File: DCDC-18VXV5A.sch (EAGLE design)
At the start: 36 parts, among them Q10 NMOSFET, Q9 NMOSFET, U1 LM3150MHX/NOPB

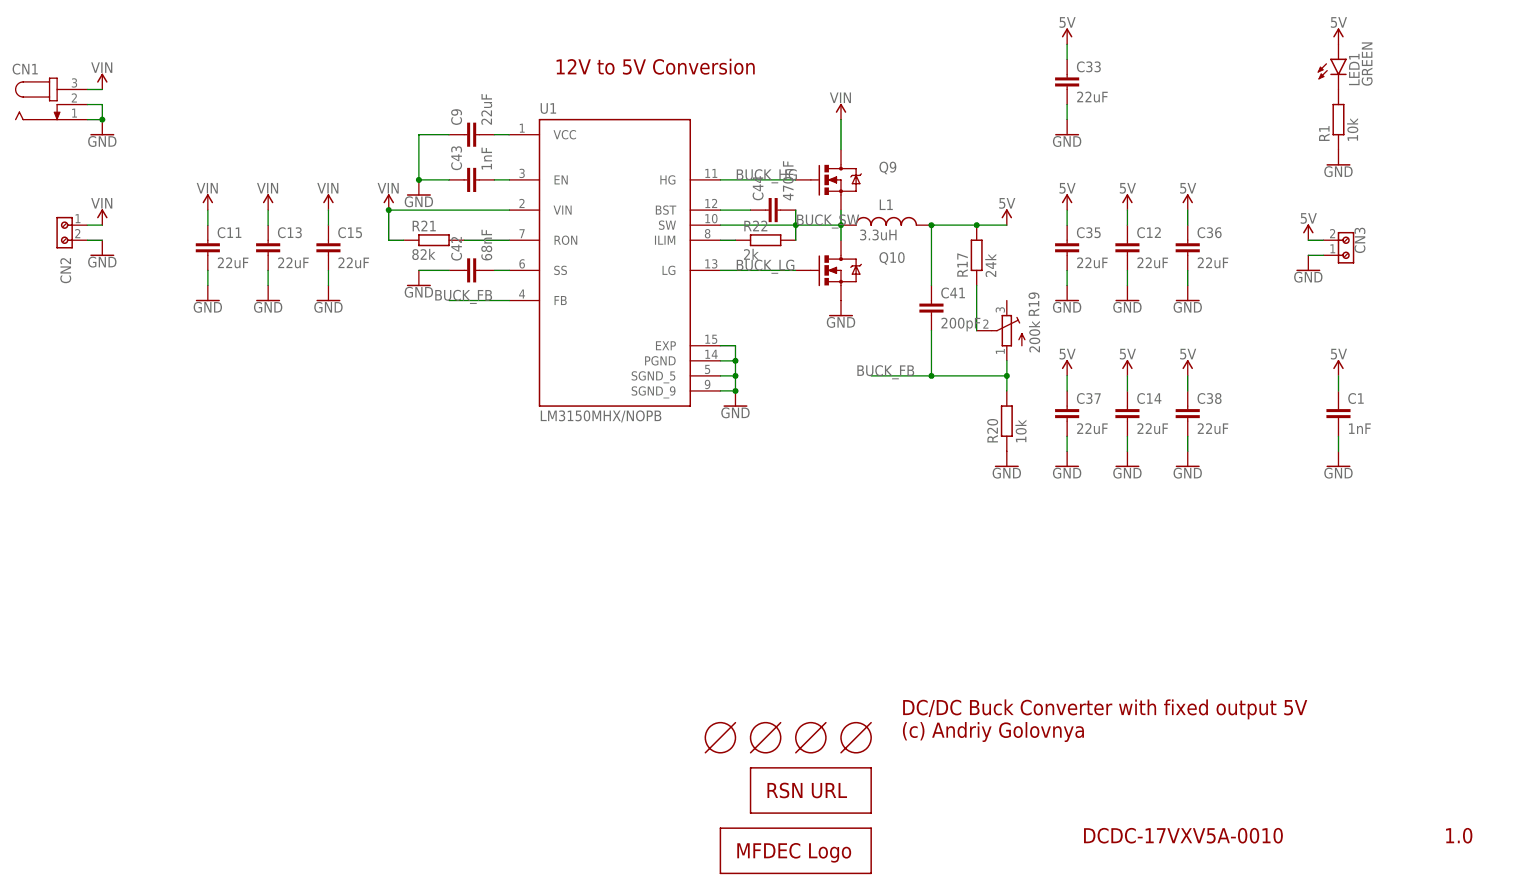
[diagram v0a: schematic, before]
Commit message: Changed texts on 18V-12V boards. Generated CAM files. Generated PNG preview. Generated PDF schematics.
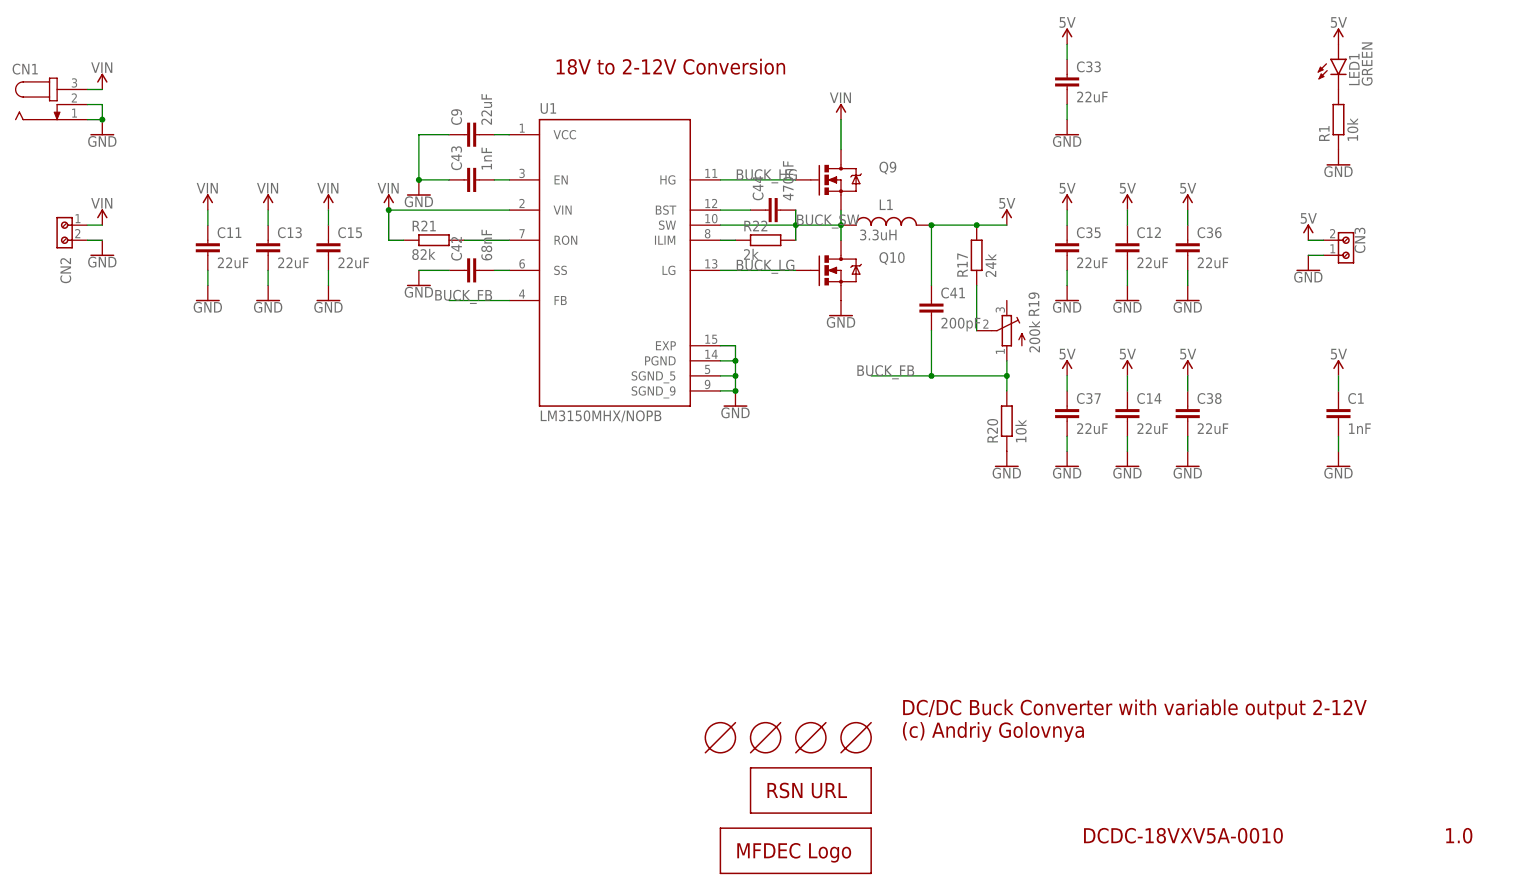
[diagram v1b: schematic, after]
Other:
- note added: "18V to 2-12V Conversion"
- note added: "DC/DC Buck Converter with variable output 2-12V (c) Andriy Golovnya"
- note added: "DCDC-18VXV5A-0010"
- note removed: "12V to 5V Conversion"
- note removed: "DC/DC Buck Converter with fixed output 5V (c) Andriy Golovnya"
- note removed: "DCDC-17VXV5A-0010"
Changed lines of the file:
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@@
 <plain>
 <text x="256.54" y="7.62" size="2.54" layer="94">1.0</text>
-<text x="195.58" y="7.62" size="2.54" layer="94">DCDC-17VXV5A-0010</text>
-<text x="165.1" y="25.4" size="2.54" layer="94">DC/DC Buck Converter with fixed output 5V
+<text x="195.58" y="7.62" size="2.54" layer="94">DCDC-18VXV5A-0010</text>
+<text x="165.1" y="25.4" size="2.54" layer="94">DC/DC Buck Converter with variable output 2-12V
 (c) Andriy Golovnya</text>
-<text x="106.68" y="137.16" size="2.54" layer="94">12V to 5V Conversion</text>
+<text x="106.68" y="137.16" size="2.54" layer="94">18V to 2-12V Conversion</text>
 </plain>
 <instances>

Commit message: Renamed VOUT line. Generated CAM files. Generated PNG preview. Generated PDF schematics.
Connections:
- net 5V renamed VOUT
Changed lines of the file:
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@@
 <part name="C37" library="rcl" library_urn="urn:adsk.eagle:library:334" deviceset="C-EU" device="C0805K" package3d_urn="urn:adsk.eagle:package:23681/2" value="22uF"/>
 <part name="C38" library="rcl" library_urn="urn:adsk.eagle:library:334" deviceset="C-EU" device="C0805K" package3d_urn="urn:adsk.eagle:package:23681/2" value="22uF"/>
-<part name="SUPPLY41" library="SparkFun-PowerSymbols" library_urn="urn:adsk.eagle:library:530" deviceset="5V" device=""/>
-<part name="SUPPLY42" library="SparkFun-PowerSymbols" library_urn="urn:adsk.eagle:library:530" deviceset="5V" device=""/>
+<part name="SUPPLY41" library="SparkFun-PowerSymbols" library_urn="urn:adsk.eagle:library:530" deviceset="VOUT" device=""/>
+<part name="SUPPLY42" library="SparkFun-PowerSymbols" library_urn="urn:adsk.eagle:library:530" deviceset="VOUT" device=""/>
 <part name="U1" library="LM3150MHX_NOPB" deviceset="LM3150MHX/NOPB" device=""/>
 <part name="Q9" library="BeagleBone_Blue_R3" library_urn="urn:adsk.eagle:library:5828899" deviceset="MOSFET-NCHANNEL" device="FDD8780" package3d_urn="urn:adsk.eagle:package:5829549/1" value="NMOSFET"/>
@@
 <part name="GND51" library="SparkFun-PowerSymbols" library_urn="urn:adsk.eagle:library:530" deviceset="GND" device=""/>
 <part name="L1" library="Wurth_Automotive_WE-CHSA" library_urn="urn:adsk.eagle:library:14076700" deviceset="WE-CHSA_1011" device="" package3d_urn="urn:adsk.eagle:package:13154812/4" technology="_7843330330" value="3.3uH"/>
-<part name="SUPPLY45" library="SparkFun-PowerSymbols" library_urn="urn:adsk.eagle:library:530" deviceset="5V" device=""/>
+<part name="SUPPLY45" library="SparkFun-PowerSymbols" library_urn="urn:adsk.eagle:library:530" deviceset="VOUT" device=""/>
 <part name="GND52" library="SparkFun-PowerSymbols" library_urn="urn:adsk.eagle:library:530" deviceset="GND" device=""/>
 <part name="SUPPLY46" library="SparkFun-PowerSymbols" library_urn="urn:adsk.eagle:library:530" deviceset="VIN" device=""/>
@@
 <part name="SUPPLY3" library="SparkFun-PowerSymbols" library_urn="urn:adsk.eagle:library:530" deviceset="VIN" device=""/>
 <part name="SUPPLY5" library="SparkFun-PowerSymbols" library_urn="urn:adsk.eagle:library:530" deviceset="VIN" device=""/>
-<part name="SUPPLY47" library="SparkFun-PowerSymbols" library_urn="urn:adsk.eagle:library:530" deviceset="5V" device=""/>
-<part name="SUPPLY48" library="SparkFun-PowerSymbols" library_urn="urn:adsk.eagle:library:530" deviceset="5V" device=""/>
-<part name="SUPPLY49" library="SparkFun-PowerSymbols" library_urn="urn:adsk.eagle:library:530" deviceset="5V" device=""/>
-<part name="SUPPLY50" library="SparkFun-PowerSymbols" library_urn="urn:adsk.eagle:library:530" deviceset="5V" device=""/>
-<part name="SUPPLY51" library="SparkFun-PowerSymbols" library_urn="urn:adsk.eagle:library:530" deviceset="5V" device=""/>
+<part name="SUPPLY47" library="SparkFun-PowerSymbols" library_urn="urn:adsk.eagle:library:530" deviceset="VOUT" device=""/>
+<part name="SUPPLY48" library="SparkFun-PowerSymbols" library_urn="urn:adsk.eagle:library:530" deviceset="VOUT" device=""/>
+<part name="SUPPLY49" library="SparkFun-PowerSymbols" library_urn="urn:adsk.eagle:library:530" deviceset="VOUT" device=""/>
+<part name="SUPPLY50" library="SparkFun-PowerSymbols" library_urn="urn:adsk.eagle:library:530" deviceset="VOUT" device=""/>
+<part name="SUPPLY51" library="SparkFun-PowerSymbols" library_urn="urn:adsk.eagle:library:530" deviceset="VOUT" device=""/>
 <part name="GND58" library="SparkFun-PowerSymbols" library_urn="urn:adsk.eagle:library:530" deviceset="GND" device=""/>
 <part name="GND59" library="SparkFun-PowerSymbols" library_urn="urn:adsk.eagle:library:530" deviceset="GND" device=""/>
@@
 <part name="SUPPLY1" library="SparkFun-PowerSymbols" library_urn="urn:adsk.eagle:library:530" deviceset="VIN" device=""/>
 <part name="GND3" library="SparkFun-PowerSymbols" library_urn="urn:adsk.eagle:library:530" deviceset="GND" device=""/>
-<part name="SUPPLY6" library="SparkFun-PowerSymbols" library_urn="urn:adsk.eagle:library:530" deviceset="5V" device=""/>
+<part name="SUPPLY6" library="SparkFun-PowerSymbols" library_urn="urn:adsk.eagle:library:530" deviceset="VOUT" device=""/>
 <part name="LOGO1" library="_my_logos" deviceset="RSNURL" device="_QR_8MM" value="RSNURL_QR_8MM"/>
 <part name="LOGO2" library="_my_logos" deviceset="MFDECLOGO" device="_L_10MM" value="MFDECLOGO_L_10MM"/>
 <part name="LED1" library="led" library_urn="urn:adsk.eagle:library:259" deviceset="LED" device="SML0603" package3d_urn="urn:adsk.eagle:package:15832/1" value="GREEN"/>
 <part name="R1" library="rcl" library_urn="urn:adsk.eagle:library:334" deviceset="R-EU_" device="R0603" package3d_urn="urn:adsk.eagle:package:23555/3" value="10k"/>
-<part name="SUPPLY7" library="SparkFun-PowerSymbols" library_urn="urn:adsk.eagle:library:530" deviceset="5V" device=""/>
+<part name="SUPPLY7" library="SparkFun-PowerSymbols" library_urn="urn:adsk.eagle:library:530" deviceset="VOUT" device=""/>
 <part name="GND4" library="SparkFun-PowerSymbols" library_urn="urn:adsk.eagle:library:530" deviceset="GND" device=""/>
 <part name="HOLE1" library="_my_fiducia" deviceset="TOOLINGHOLE" device=""/>
@@
 <part name="HOLE3" library="_my_fiducia" deviceset="TOOLINGHOLE" device=""/>
 <part name="C1" library="rcl" library_urn="urn:adsk.eagle:library:334" deviceset="C-EU" device="C0603K" package3d_urn="urn:adsk.eagle:package:23680/2" value="1nF"/>
-<part name="SUPPLY9" library="SparkFun-PowerSymbols" library_urn="urn:adsk.eagle:library:530" deviceset="5V" device=""/>
+<part name="SUPPLY9" library="SparkFun-PowerSymbols" library_urn="urn:adsk.eagle:library:530" deviceset="VOUT" device=""/>
 <part name="GND5" library="SparkFun-PowerSymbols" library_urn="urn:adsk.eagle:library:530" deviceset="GND" device=""/>
 <part name="SUPPLY4" library="SparkFun-PowerSymbols" library_urn="urn:adsk.eagle:library:530" deviceset="VIN" device=""/>
@@
 </segment>
 </net>
-<net name="5V" class="0">
+<net name="VOUT" class="0">
 <segment>
 <pinref part="C36" gate="G$1" pin="1"/>
 <wire x1="213.36" y1="111.76" x2="213.36" y2="114.3" width="0.1524" layer="91"/>
-<pinref part="SUPPLY42" gate="G$1" pin="5V"/>
+<pinref part="SUPPLY42" gate="G$1" pin="VOUT"/>
 </segment>
 <segment>
 <pinref part="C38" gate="G$1" pin="1"/>
 <wire x1="213.36" y1="83.82" x2="213.36" y2="86.36" width="0.1524" layer="91"/>
-<pinref part="SUPPLY41" gate="G$1" pin="5V"/>
+<pinref part="SUPPLY41" gate="G$1" pin="VOUT"/>
 </segment>
 <segment>
 <pinref part="L1" gate="G$1" pin="2"/>
-<pinref part="SUPPLY45" gate="G$1" pin="5V"/>
+<pinref part="SUPPLY45" gate="G$1" pin="VOUT"/>
 <pinref part="R17" gate="G$1" pin="2"/>
 <wire x1="170.18" y1="111.76" x2="177.8" y2="111.76" width="0.1524" layer="91"/>
@@
 <pinref part="C33" gate="G$1" pin="1"/>
 <wire x1="193.04" y1="142.24" x2="193.04" y2="139.7" width="0.1524" layer="91"/>
-<pinref part="SUPPLY47" gate="G$1" pin="5V"/>
+<pinref part="SUPPLY47" gate="G$1" pin="VOUT"/>
 </segment>
 <segment>
 <pinref part="C12" gate="G$1" pin="1"/>
 <wire x1="203.2" y1="114.3" x2="203.2" y2="111.76" width="0.1524" layer="91"/>
-<pinref part="SUPPLY48" gate="G$1" pin="5V"/>
+<pinref part="SUPPLY48" gate="G$1" pin="VOUT"/>
 </segment>
 <segment>
 <pinref part="C35" gate="G$1" pin="1"/>
 <wire x1="193.04" y1="114.3" x2="193.04" y2="111.76" width="0.1524" layer="91"/>
-<pinref part="SUPPLY49" gate="G$1" pin="5V"/>
+<pinref part="SUPPLY49" gate="G$1" pin="VOUT"/>
 </segment>
 <segment>
 <pinref part="C14" gate="G$1" pin="1"/>
 <wire x1="203.2" y1="86.36" x2="203.2" y2="83.82" width="0.1524" layer="91"/>
-<pinref part="SUPPLY50" gate="G$1" pin="5V"/>
+<pinref part="SUPPLY50" gate="G$1" pin="VOUT"/>
 </segment>
 <segment>
 <pinref part="C37" gate="G$1" pin="1"/>
 <wire x1="193.04" y1="86.36" x2="193.04" y2="83.82" width="0.1524" layer="91"/>
-<pinref part="SUPPLY51" gate="G$1" pin="5V"/>
-</segment>
-<segment>
-<pinref part="SUPPLY6" gate="G$1" pin="5V"/>
+<pinref part="SUPPLY51" gate="G$1" pin="VOUT"/>
+</segment>
+<segment>
+<pinref part="SUPPLY6" gate="G$1" pin="VOUT"/>
 <pinref part="CN3" gate="G$1" pin="2"/>
 <wire x1="233.68" y1="109.22" x2="236.22" y2="109.22" width="0.1524" layer="91"/>
@@
 <segment>
 <pinref part="LED1" gate="G$1" pin="A"/>
-<pinref part="SUPPLY7" gate="G$1" pin="5V"/>
+<pinref part="SUPPLY7" gate="G$1" pin="VOUT"/>
 </segment>
 <segment>
 <pinref part="C1" gate="G$1" pin="1"/>
-<pinref part="SUPPLY9" gate="G$1" pin="5V"/>
+<pinref part="SUPPLY9" gate="G$1" pin="VOUT"/>
 <wire x1="238.76" y1="83.82" x2="238.76" y2="86.36" width="0.1524" layer="91"/>
 </segment>
